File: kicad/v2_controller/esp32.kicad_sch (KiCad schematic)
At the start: 9 parts, among them J3 Conn_02x10_Odd_Even, J4 Conn_02x10_Odd_Even, U1 ESP32-S3-WROOM-1-N16R8, U6 74AHCT1G125

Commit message: [kicad] additional work on v2 controller
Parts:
- added C? (x4): 1uF, Capacitor_SMD:C_0402_1005Metric, symbol Device:C
- added C? (x2): 10uF, Capacitor_SMD:C_0603_1608Metric, symbol Device:C
- added R2: 390k, Resistor_SMD:R_0603_1608Metric, symbol Device:R
- added R4, R5: 4.7k, Resistor_SMD:R_0402_1005Metric, symbol Device:R
- added R?: 10k, Resistor_SMD:R_0402_1005Metric, symbol Device:R
- added SW18, SW19: SW_MEC_5E, Button_Switch_SMD:SW_Push_1P1T_XKB_TS-1187A, symbol Switch:SW_MEC_5E
- added U2: SSD1306_I2C, mantyl:SSD1306_OLED-0.91-128x32_Back_Mount, symbol mantyl:SSD1306_I2C
- U3: renamed from U6; footprint (none) -> Package_TO_SOT_SMD:SOT-353_SC-70-5; LCSC Part # (none) -> C151417
- renumbered C2 to C?, C1 to C?, C3 to C?, J3 to J1, J4 to J2, R1 to R?, U1 to U?
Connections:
- net CHIP_PU: now also SW19.3 (K)
- net COL0: now also U?.15 (GPIO3)
- net COL1: now also U?.16 (GPIO46)
- net COL2: now also U?.17 (GPIO9)
- net COL3: now also U?.18 (GPIO10)
- net COL4: now also U?.19 (GPIO11)
- net COL5: now also U?.20 (GPIO12)
- net COL6: now also U?.21 (GPIO13)
- net COL7: now also U?.22 (GPIO14)
- net COL8: now also U?.23 (GPIO21)
- net COL9: now also U?.24 (GPIO47/SPICLK_P)
- net ESP_3V3: now also C?.2, C?.2, R4.1, R5.1, R?.1, U2.5 (VBAT), U2.8 (VDD)
- net GND: now also C?.1, C?.1, C?.2, C?.2, R2.2, SW18.1, SW19.1, U2.7 (VSS)
- net GPIO0: now also SW18.3 (K)
- net LED_NUMPAD_DIN_3V3: now also U?.29 (GPIO36)
- net ROW0: now also U?.4 (GPIO4)
- net ROW1: now also U?.5 (GPIO5)
- net ROW10: now also U?.31 (GPIO38)
- net ROW11: now also U?.30 (GPIO37)
- net ROW2: now also U?.6 (GPIO6)
- net ROW3: now also U?.7 (GPIO7)
- net ROW4: now also U?.8 (GPIO15/XTAL_32K_P)
- net ROW5: now also U?.9 (GPIO16/XTAL_32K_N)
- net ROW6: now also U?.35 (GPIO42)
- net ROW7: now also U?.34 (GPIO41)
- net ROW8: now also U?.33 (GPIO40)
- net ROW9: now also U?.32 (GPIO39)
- net SCL: now also U?.39 (GPIO1), R4.2, U2.10 (SCL)
- net SDA: now also U?.38 (GPIO2), R5.2, U2.11 (SDA)
- net SSD1306_RST: now reaches U?.28 (GPIO35)
- net SSD1306_RST: now also R?.2, U2.9 (RES#)
- new net: C?.1, U2.2 (C2N)
- new net: C?.2, U2.1 (C2P)
- new net: R2.1, U2.12 (IREF)
- new net: C?.1, U2.13 (VCOMH)
- new net: C?.1, U2.14 (VCC)
- new net: C?.2, U2.3 (C1P)
- new net: C?.1, U2.4 (C1N)
- no-connect marks 3 -> 11
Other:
- note added: "ESP32-S3"
- note added: "Headers"
- note added: "Level Shifter"
- note added: "OLED Display"
- note added: "Power Buttons"
- moved on the sheet: C?, J1, J2, U3

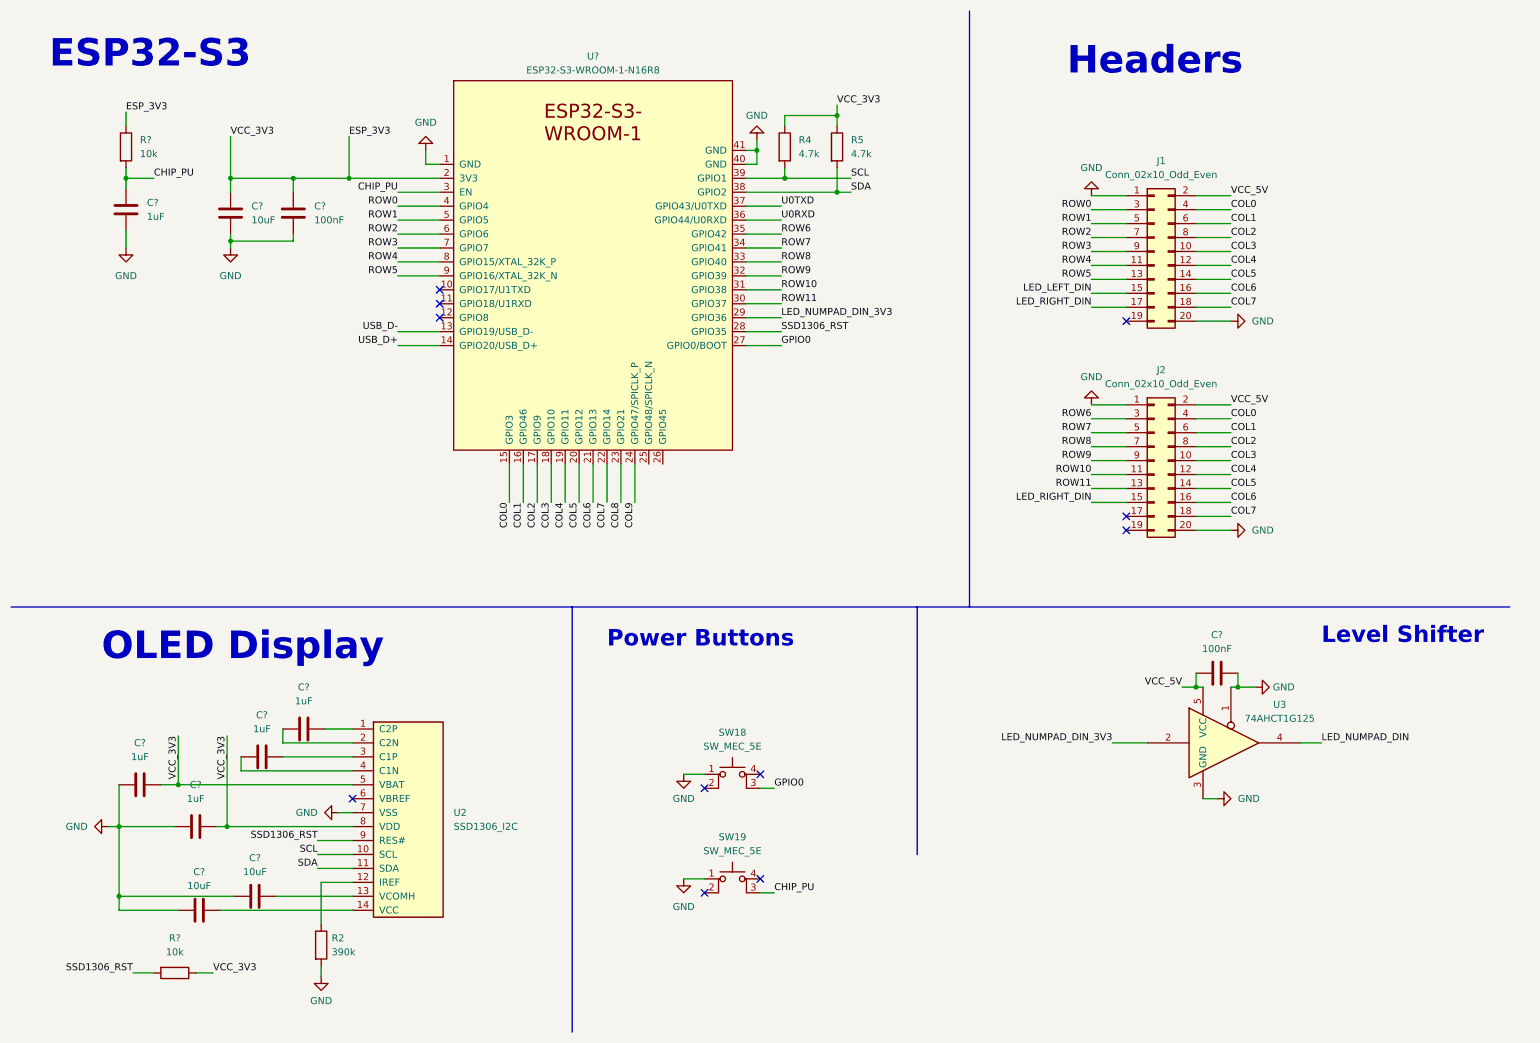
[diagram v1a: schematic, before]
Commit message: [kicad] fix global symbol usage in v2 controller
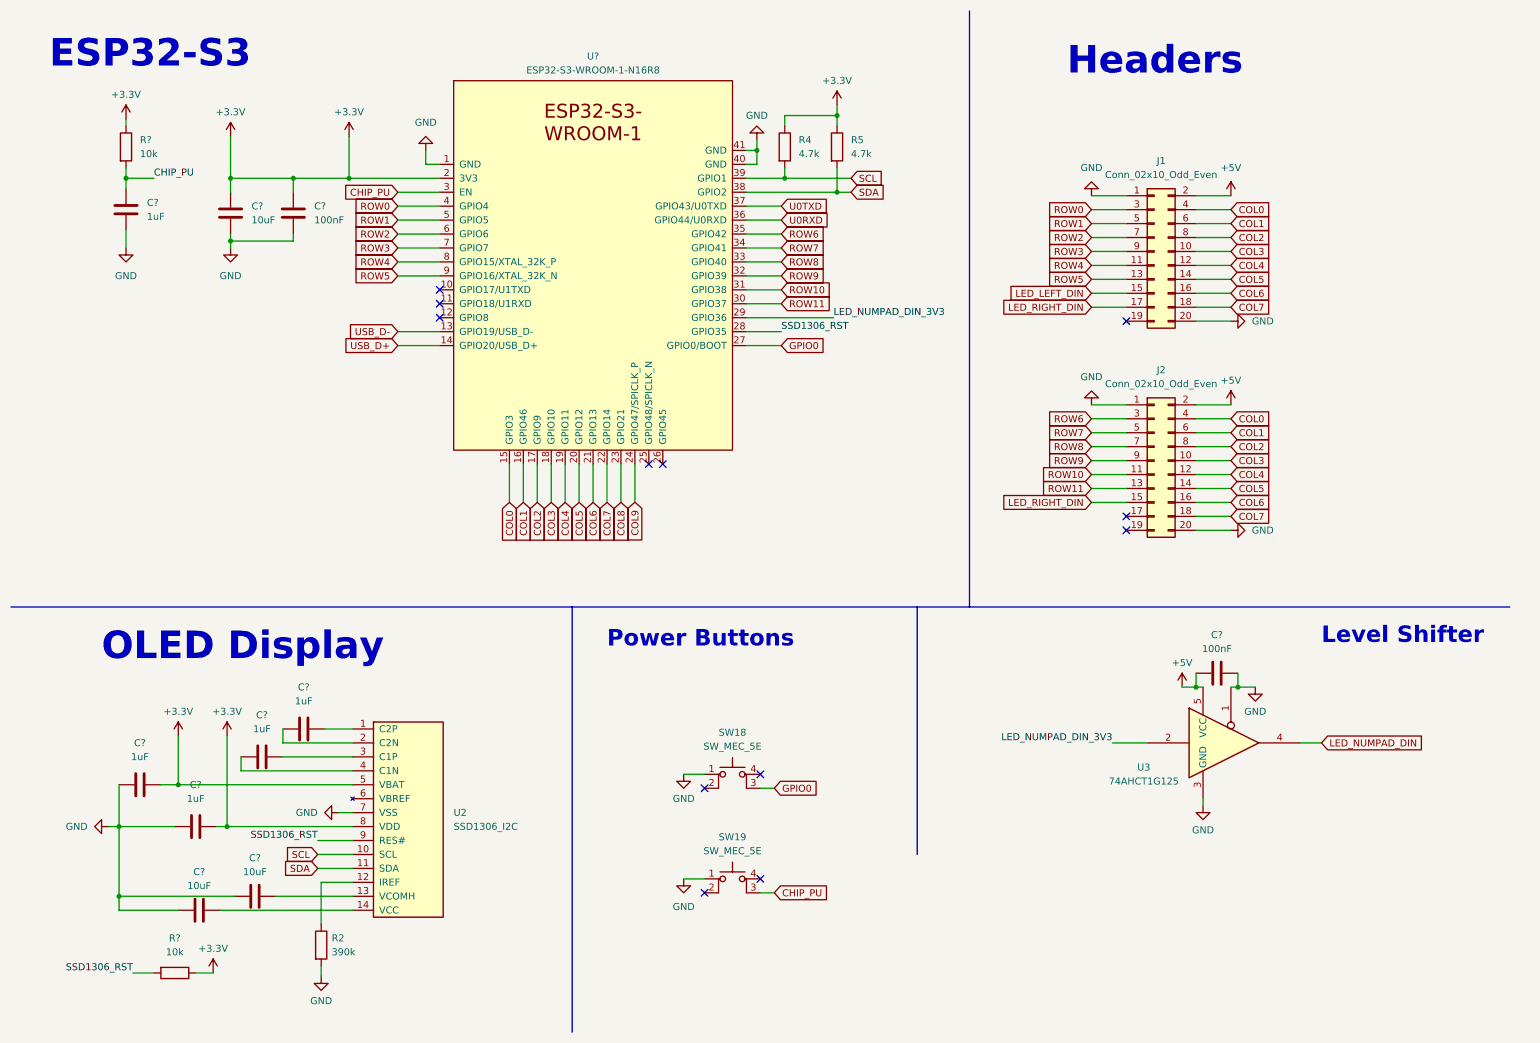
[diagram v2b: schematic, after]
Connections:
- net ESP_3V3 renamed +3.3V
- net VCC_5V renamed +5V
- no-connect marks 11 -> 12

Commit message: [kicad] update v2 controller to use hierarchical labels
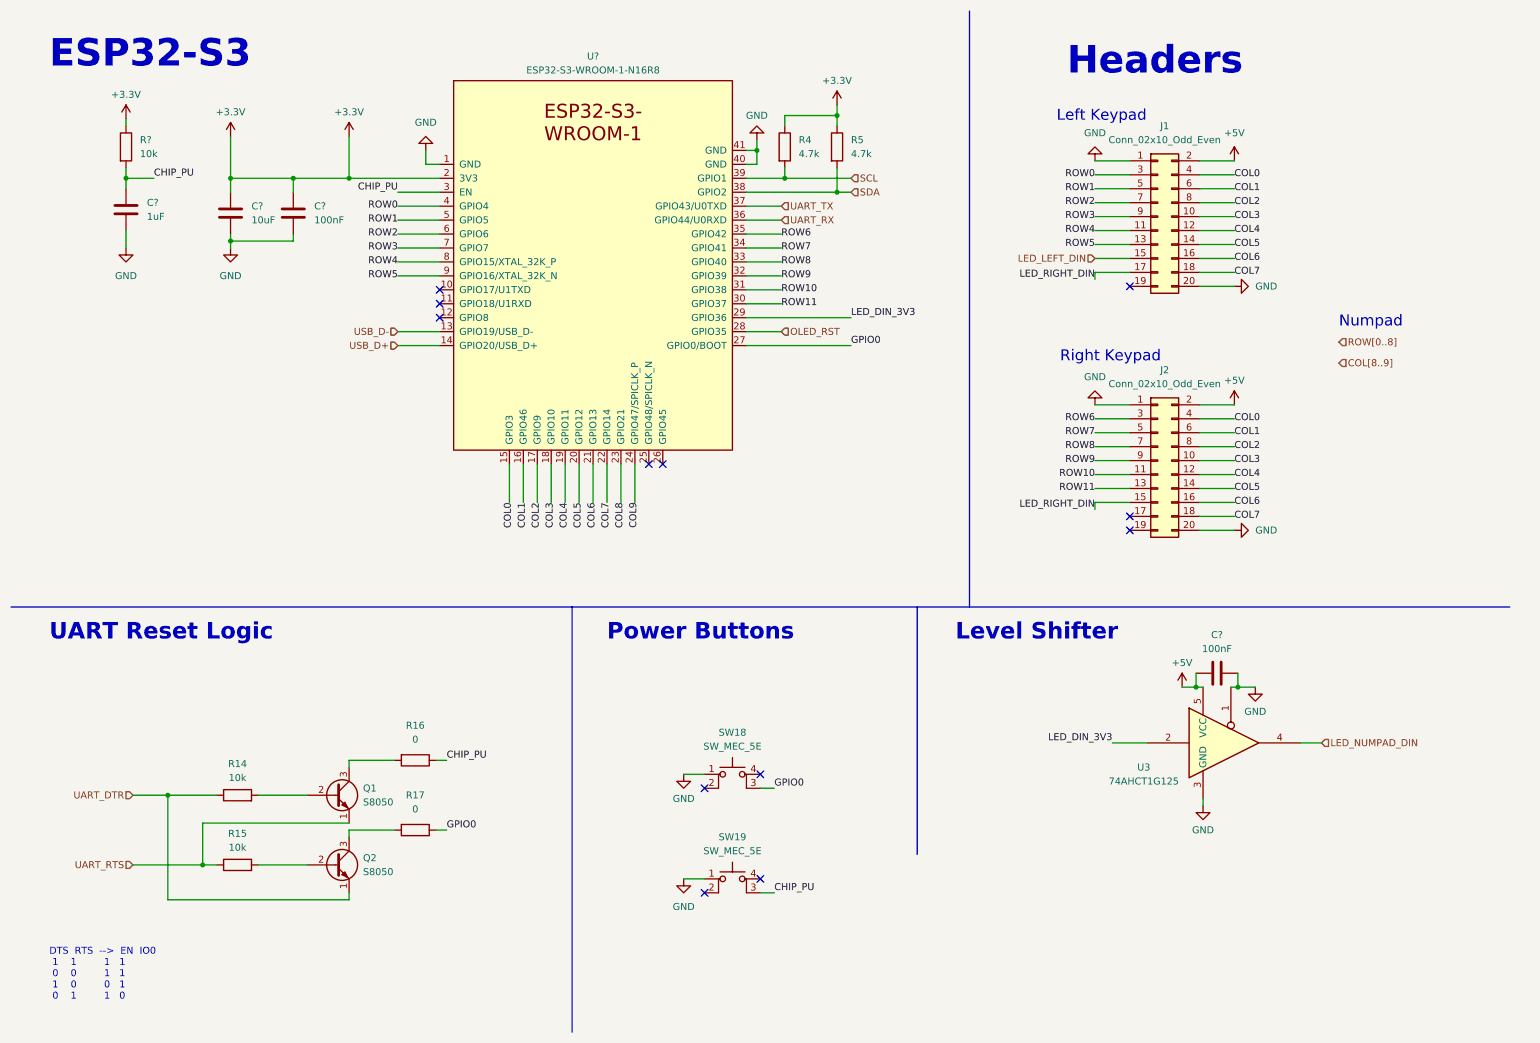
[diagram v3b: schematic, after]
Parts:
- removed C? (x4): 1uF, Capacitor_SMD:C_0402_1005Metric, symbol Device:C
- removed C? (x2): 10uF, Capacitor_SMD:C_0603_1608Metric, symbol Device:C
- removed R2: 390k, Resistor_SMD:R_0603_1608Metric, symbol Device:R
- removed R?: 10k, Resistor_SMD:R_0402_1005Metric, symbol Device:R
- removed U2: SSD1306_I2C, mantyl:SSD1306_OLED-0.91-128x32_Back_Mount, symbol mantyl:SSD1306_I2C
- added Q1, Q2: S8050, Package_TO_SOT_SMD:SOT-23, symbol Transistor_BJT:S8050
- added R14, R15: 10k, Resistor_SMD:R_0402_1005Metric, symbol Device:R
- added R16, R17: 0, Resistor_SMD:R_0402_1005Metric, symbol Device:R
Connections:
- net CHIP_PU: now also R16.1
- net GPIO0: now also R17.1
- net LED_NUMPAD_DIN_3V3 renamed LED_DIN_3V3
- net SSD1306_RST renamed OLED_RST
- net U0RXD renamed UART_RX
- net U0TXD renamed UART_TX
- new net: Q1.2 (B), R14.2
- new net: Q1.3 (C), R16.2
- new net: Q2.2 (B), R15.2
- new net: Q2.3 (C), R17.2
- new net UART_DTR: Q2.1 (E), R14.1
- new net UART_RTS: Q1.1 (E), R15.1
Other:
- note added: "DTS RTS --> EN IO0 1 1 1 1 0 0 1 1 1 0 0 1 0 1 1 0"
- note added: "Left Keypad"
- note added: "Numpad"
- note added: "Right Keypad"
- note added: "UART Reset Logic"
- note removed: "OLED Display"
- moved on the sheet: J1, J2

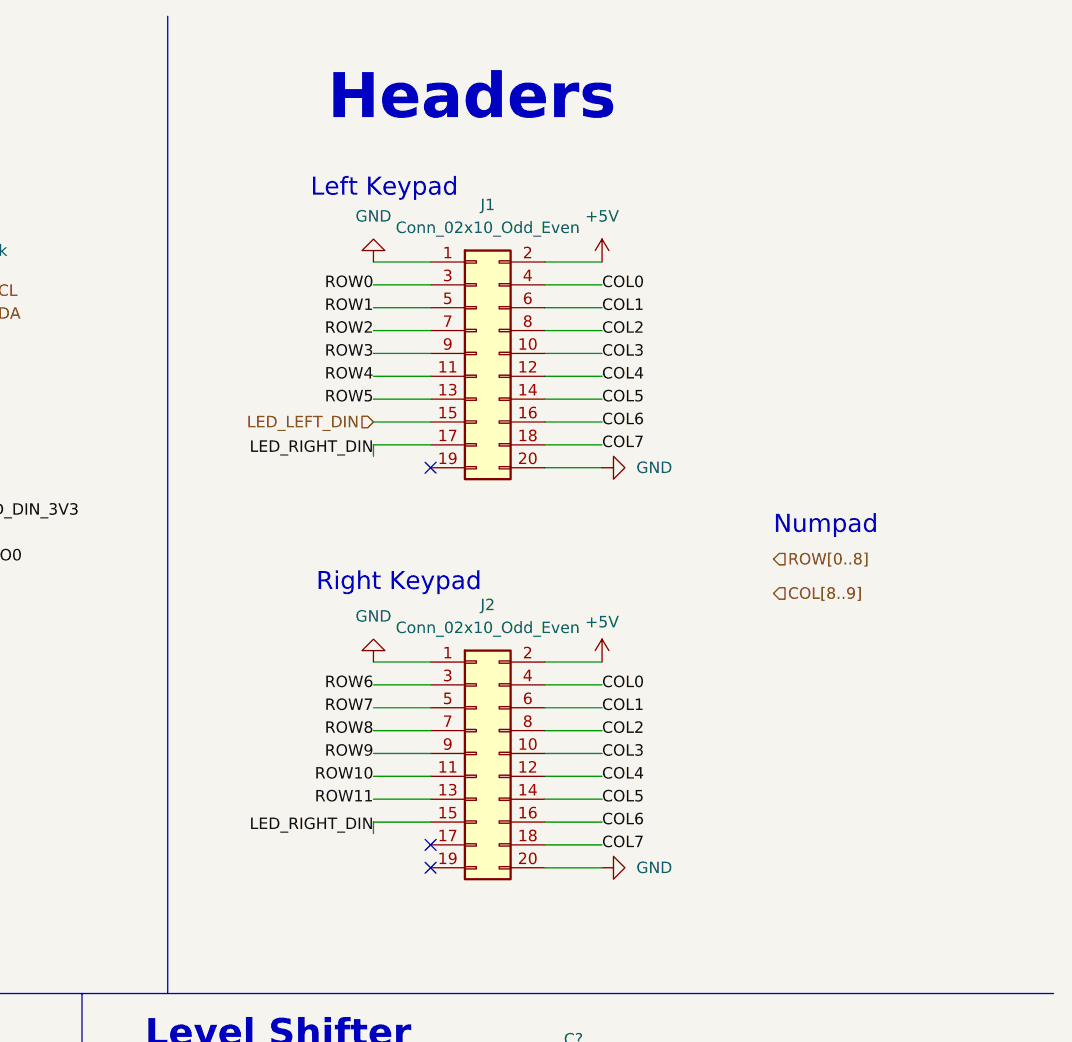
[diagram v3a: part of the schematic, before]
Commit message: [kicad] add a debug header to the v2 controller
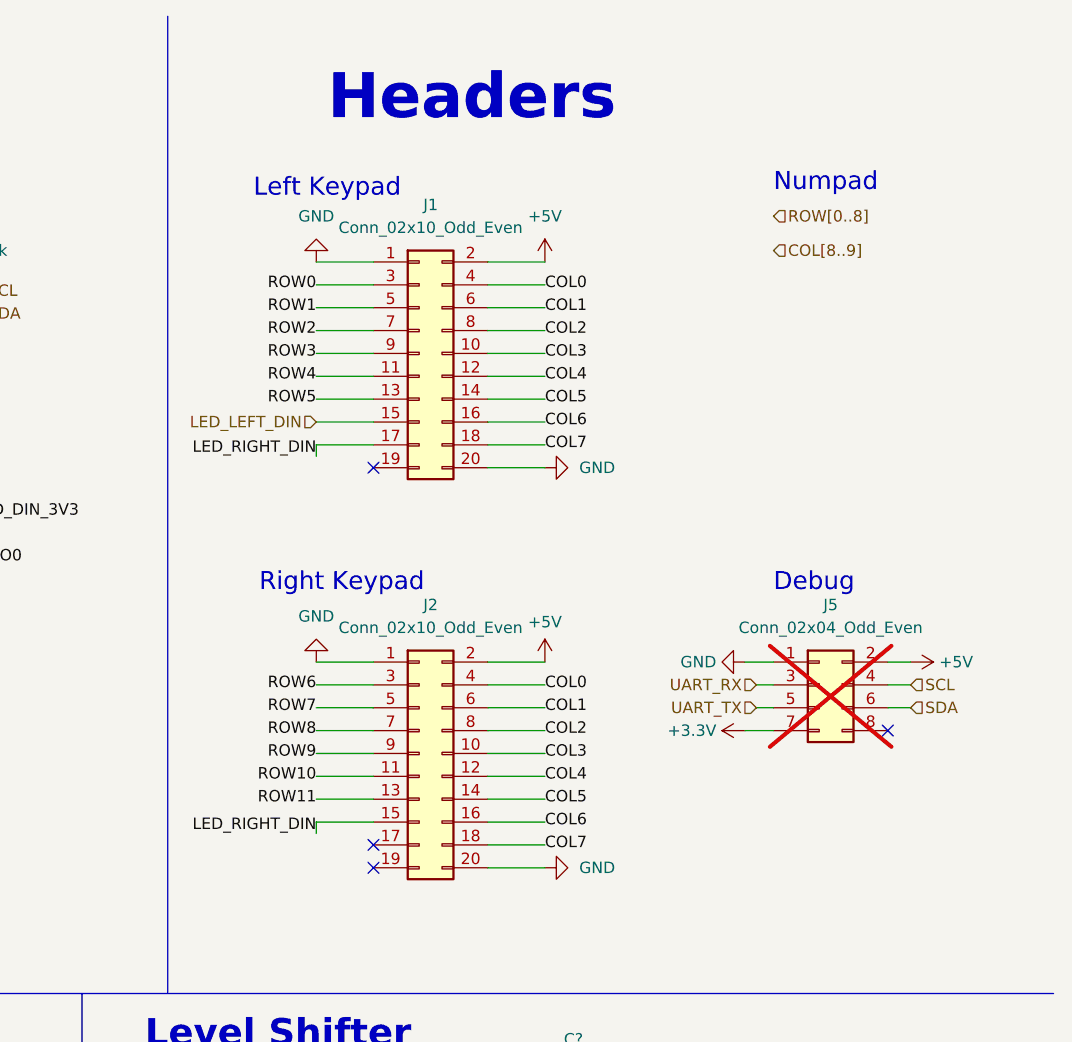
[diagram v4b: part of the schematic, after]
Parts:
- added J5: Conn_02x04_Odd_Even, Connector_PinHeader_2.54mm:PinHeader_2x04_P2.54mm_Vertical, symbol Connector_Generic:Conn_02x04_Odd_Even
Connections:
- net +3.3V: now also J5.7 (Pin_7)
- net +5V: now also J5.2 (Pin_2)
- net GND: now also J5.1 (Pin_1)
- net SCL: now also J5.4 (Pin_4)
- net SDA: now also J5.6 (Pin_6)
- net UART_RX: now also J5.3 (Pin_3)
- net UART_TX: now also J5.5 (Pin_5)
- no-connect marks 12 -> 13
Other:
- note added: "Debug"
- moved on the sheet: J1, J2
